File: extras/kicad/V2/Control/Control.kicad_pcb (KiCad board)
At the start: 2 copper layers, 181.3 x 110 mm, 43 parts, among them J1 Ultrasonic Ranging, J2 Conn_01x05, J3 Output, J4 Input, J6 left, J7 right, P8 BeagleBone_Black_Header, P9 BeagleBone_Black_Header, U1 SparkFun-micromod, U2 ESP-01-WIFI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

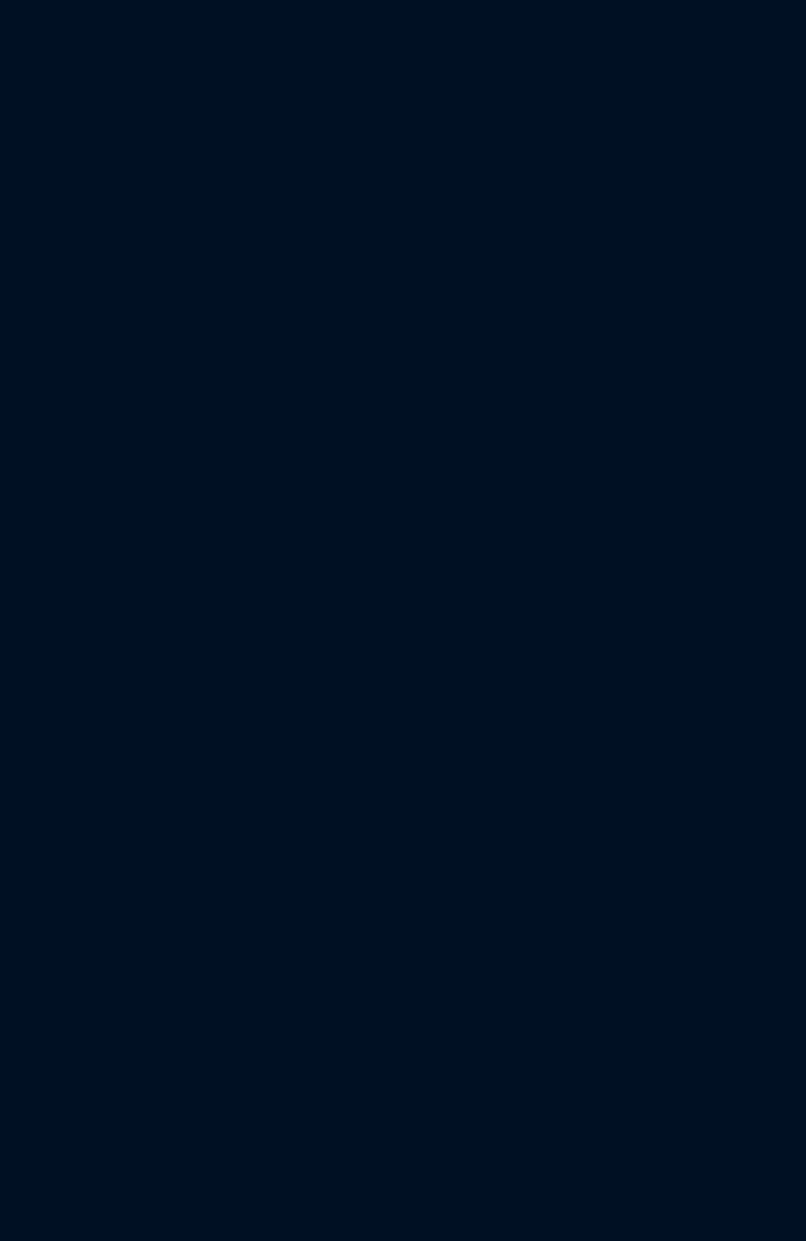
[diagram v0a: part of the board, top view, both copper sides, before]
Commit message: added 2242 footprint
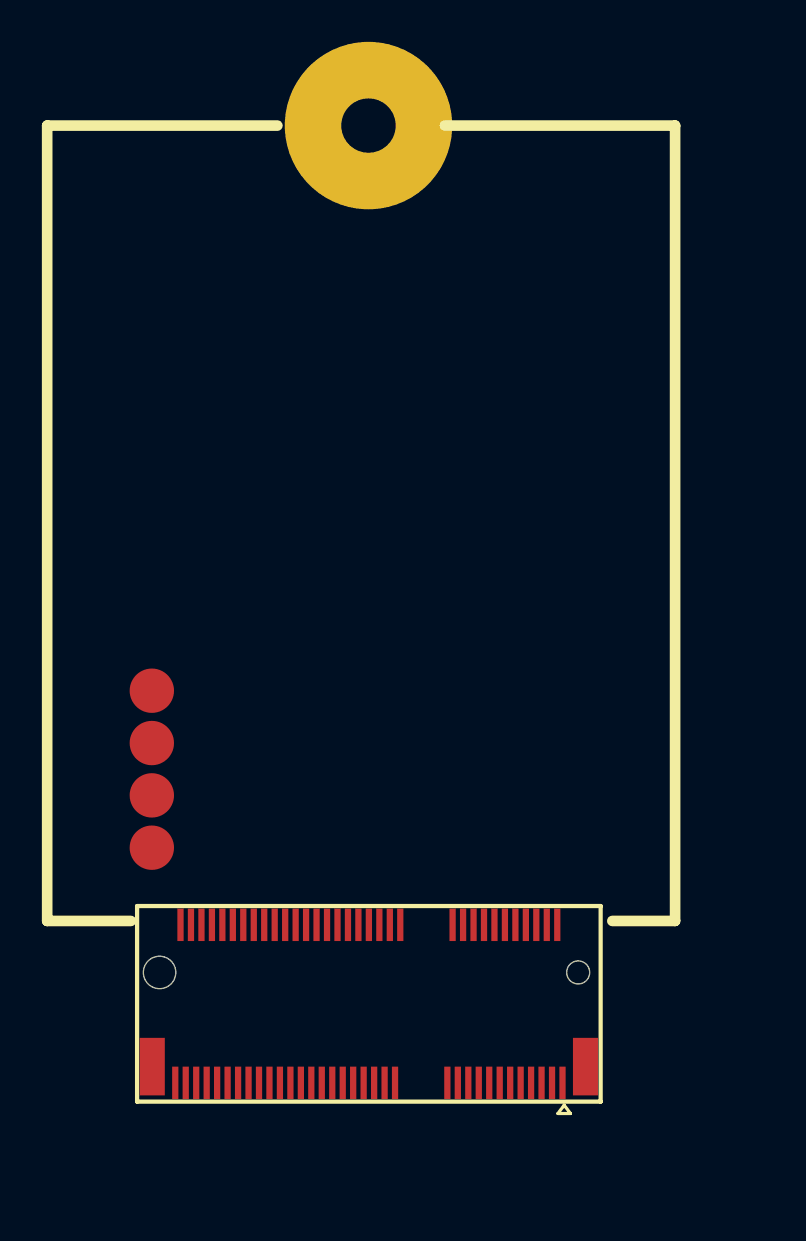
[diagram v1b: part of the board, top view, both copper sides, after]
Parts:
- added ?: , clipboard:dc186f10-f96b-48f3-81b4-f4aa225eb881, F.Cu at (2.54, -25.4)
